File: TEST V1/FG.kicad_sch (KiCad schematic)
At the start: 34 parts, among them U10 MCP4725A2T-ECH, U2 AD9833, U3 LM318N, U4 LM318N, Y3 25 MHz

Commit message: Integrated FG, RPS, and PCB updates
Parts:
- C26: renamed from C12; footprint (none) -> Capacitor_SMD:C_0603_1608Metric_Pad1.08x0.95mm_HandSolder
- C27: renamed from C11; footprint (none) -> Capacitor_SMD:C_0603_1608Metric_Pad1.08x0.95mm_HandSolder
- C28: renamed from C6; footprint (none) -> Capacitor_SMD:C_0603_1608Metric_Pad1.08x0.95mm_HandSolder
- C29: renamed from C40; footprint (none) -> Capacitor_SMD:C_0603_1608Metric_Pad1.08x0.95mm_HandSolder
- C30: renamed from C9; footprint (none) -> Capacitor_SMD:C_0603_1608Metric_Pad1.08x0.95mm_HandSolder
- C31: renamed from C5; footprint (none) -> Capacitor_SMD:C_0603_1608Metric_Pad1.08x0.95mm_HandSolder
- C32: renamed from C10; footprint (none) -> Capacitor_SMD:C_0603_1608Metric_Pad1.08x0.95mm_HandSolder
- C33: renamed from C41; footprint (none) -> Capacitor_SMD:C_0603_1608Metric_Pad1.08x0.95mm_HandSolder
- C34: renamed from C8; footprint (none) -> Capacitor_SMD:C_0603_1608Metric_Pad1.08x0.95mm_HandSolder
- C35: renamed from C7; footprint (none) -> Capacitor_SMD:C_0603_1608Metric_Pad1.08x0.95mm_HandSolder
- C36: renamed from C20; footprint (none) -> Capacitor_SMD:C_0603_1608Metric_Pad1.08x0.95mm_HandSolder
- C37: renamed from C21; footprint (none) -> Capacitor_SMD:C_0603_1608Metric_Pad1.08x0.95mm_HandSolder
- R41: renamed from R10; footprint (none) -> Resistor_SMD:R_0603_1608Metric_Pad0.98x0.95mm_HandSolder
- R42: renamed from R2; footprint (none) -> Resistor_SMD:R_0603_1608Metric_Pad0.98x0.95mm_HandSolder
- R43: renamed from R1; footprint (none) -> Resistor_SMD:R_0603_1608Metric_Pad0.98x0.95mm_HandSolder
- R44: renamed from R9; footprint (none) -> Resistor_SMD:R_0603_1608Metric_Pad0.98x0.95mm_HandSolder
- R45: renamed from R57; footprint (none) -> Resistor_SMD:R_0603_1608Metric_Pad0.98x0.95mm_HandSolder
- R46: renamed from R14; footprint (none) -> Resistor_SMD:R_0603_1608Metric_Pad0.98x0.95mm_HandSolder
- R47: renamed from R12; footprint (none) -> Resistor_SMD:R_0603_1608Metric_Pad0.98x0.95mm_HandSolder
- R48: renamed from R7; footprint (none) -> Resistor_SMD:R_0603_1608Metric_Pad0.98x0.95mm_HandSolder
- R49: renamed from R8; footprint (none) -> Resistor_SMD:R_0603_1608Metric_Pad0.98x0.95mm_HandSolder
- R50: renamed from R4; footprint (none) -> Resistor_SMD:R_0603_1608Metric_Pad0.98x0.95mm_HandSolder
- R51: renamed from R3; footprint (none) -> Resistor_SMD:R_0603_1608Metric_Pad0.98x0.95mm_HandSolder
- R52: renamed from R13; footprint (none) -> Resistor_SMD:R_0603_1608Metric_Pad0.98x0.95mm_HandSolder
- R53: renamed from R6; footprint (none) -> Resistor_SMD:R_0603_1608Metric_Pad0.98x0.95mm_HandSolder
- R54: renamed from R11; footprint (none) -> Resistor_SMD:R_0603_1608Metric_Pad0.98x0.95mm_HandSolder
- R55: renamed from R5; footprint (none) -> Resistor_SMD:R_0603_1608Metric_Pad0.98x0.95mm_HandSolder
- R56: renamed from R26; footprint (none) -> Resistor_SMD:R_0603_1608Metric_Pad0.98x0.95mm_HandSolder
- renumbered U3 to U7, U2 to U8, U4 to U9, Y3 to Y2

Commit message: updated RPS schematic
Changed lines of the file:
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@@
 		)
 	)
+	(global_label "-12V"
+		(shape input)
+		(at 35.56 147.32 270)
+		(fields_autoplaced yes)
+		(effects
+			(font
+				(size 1.27 1.27)
+			)
+			(justify right)
+		)
+		(property "Intersheetrefs" "${INTERSHEET_REFS}"
+			(at 35.56 155.3852 90)
+			(effects
+				(font
+					(size 1.27 1.27)
+				)
+				(justify right)
+				(hide yes)
+			)
+		)
+	)
 	(global_label "5V"
 		(shape input)
@@
 		)
 	)
+	(global_label "3v3"
+		(shape input)
+		(at 107.95 25.4 0)
+		(fields_autoplaced yes)
+		(effects
+			(font
+				(size 1.27 1.27)
+			)
+			(justify left)
+		)
+		(property "Intersheetrefs" "${INTERSHEET_REFS}"
+			(at 114.3218 25.4 0)
+			(effects
+				(font
+					(size 1.27 1.27)
+				)
+				(justify left)
+				(hide yes)
+			)
+		)
+	)
 	(global_label "SPI_EN"
 		(shape output)
@@
 		(dnp no)
 		(property "Reference" "R41"
-			(at 37.084 149.352 90)
+			(at 42.164 145.034 90)
 			(effects
 				(font

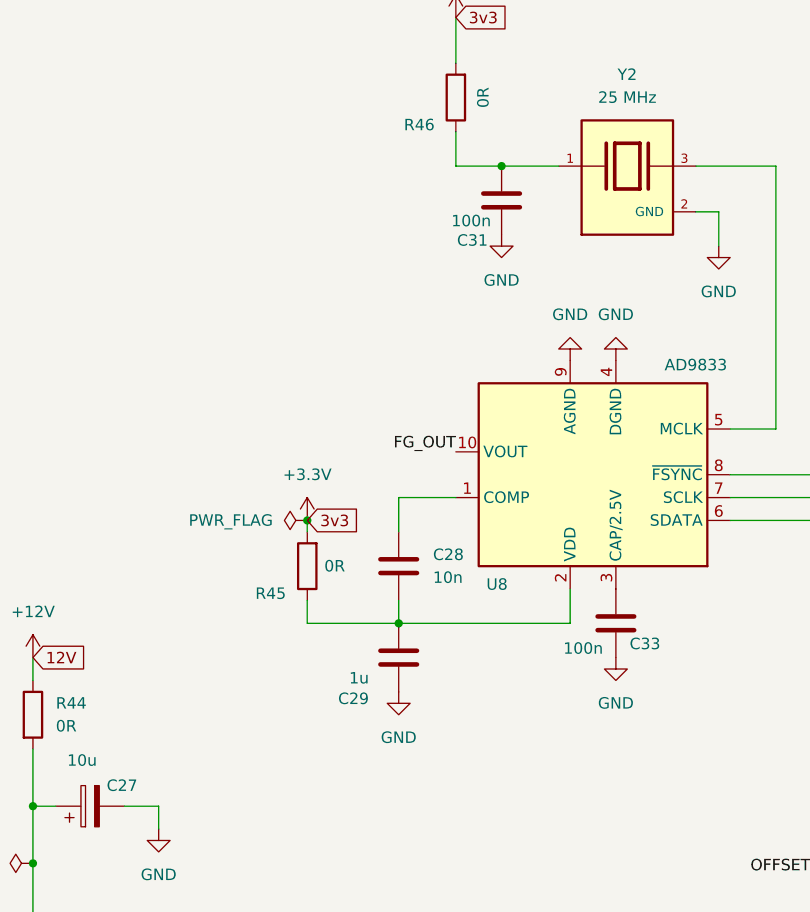
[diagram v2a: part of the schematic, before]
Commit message: updated schematic of FG
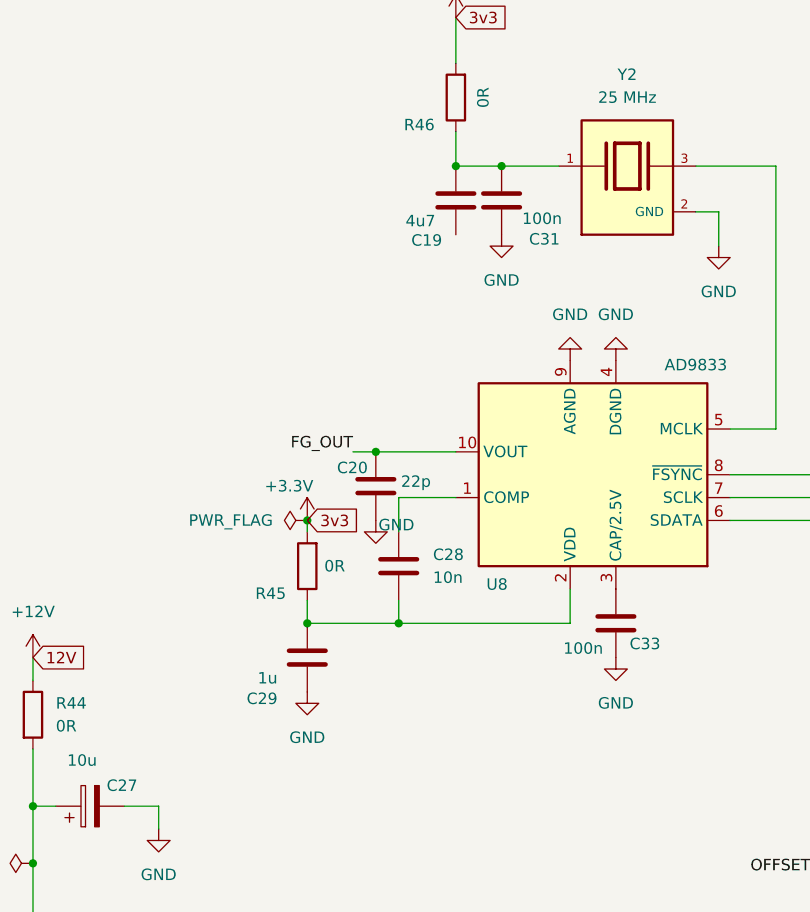
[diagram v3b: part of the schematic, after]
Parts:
- added C19: 4u7, Capacitor_SMD:C_0603_1608Metric_Pad1.08x0.95mm_HandSolder, symbol Device:C
- added C20: 22p, Capacitor_SMD:C_0603_1608Metric_Pad1.08x0.95mm_HandSolder, symbol Device:C
- RV1: footprint (none) -> Potentiometer_THT:Potentiometer_Bourns_3386X_Horizontal
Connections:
- net FG_OUT: now also C20.2
- net GND: now also C20.1
- net at C31.2, R46.1, Y2.1: now also C19.2
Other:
- moved on the sheet: C29

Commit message: updated RPS sch
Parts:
- added J16: Conn_Coaxial, symbol Connector:Conn_Coaxial
- renumbered C26 to C21, C27 to C22, C29 to C23, C20 to C24, C28 to C25, C19 to C26, C30 to C27, C31 to C28, C32 to C29, C33 to C30, C34 to C31, C35 to C32, C36 to C33, C37 to C34, R41 to R31, R42 to R32, R43 to R33, R44 to R34, R45 to R35, R46 to R36, R47 to R37, R48 to R38, R49 to R39, R50 to R40, R51 to R41, R52 to R42, R53 to R43, R54 to R44, R55 to R45, R56 to R46, U7 to U5, U8 to U6, U9 to U7, U10 to U8
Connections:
- net GND: now also C26.1, J16.2 (Ext)
- net U4_VOUT: now also J16.1 (In)

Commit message: minor changes
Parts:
- removed J16: Conn_Coaxial, symbol Connector:Conn_Coaxial
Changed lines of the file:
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@@
 	)
 	(label "U4_VOUT"
-		(at 200.66 135.89 90)
+		(at 200.66 135.89 0)
 		(effects
 			(font
@@
 	)
 	(symbol
-		(lib_id "power:GND")
-		(at 205.74 140.97 0)
-		(unit 1)
-		(exclude_from_sim no)
-		(in_bom yes)
-		(on_board yes)
-		(dnp no)
-		(property "Reference" "#PWR088"
-			(at 205.74 147.32 0)
-			(effects
-				(font
-					(size 1.27 1.27)
-				)
-				(hide yes)
-			)
-		)
-		(property "Value" "GND"
-			(at 201.93 142.748 0)
-			(effects
-				(font
-					(size 1.27 1.27)
-				)
-			)
-		)
-		(property "Footprint" ""
-			(at 205.74 140.97 0)
-			(effects
-				(font
-					(size 1.27 1.27)
-				)
-				(hide yes)
-			)
-		)
-		(property "Datasheet" ""
-			(at 205.74 140.97 0)
-			(effects
-				(font
-					(size 1.27 1.27)
-				)
-				(hide yes)
-			)
-		)
-		(property "Description" "Power symbol creates a global label with name \"GND\" , ground"
-			(at 205.74 140.97 0)
-			(effects
-				(font
-					(size 1.27 1.27)
-				)
-				(hide yes)
-			)
-		)
-		(pin "1"
-		)
-		(instances
-			(project "TEST V1"
-				(path "/e198004f-db65-4a52-ae89-6b1c9a9775ee/67a157b6-1f41-4621-8fe4-10cef685d6f6"
-					(reference "#PWR088")
-					(unit 1)
-				)
-			)
-		)
-	)
-	(symbol
 		(lib_id "Device:R")
 		(at 91.44 86.36 180)
@@
 					(unit 1)
 				)
-			)
-		)
-	)
-	(symbol
-		(lib_id "Connector:Conn_Coaxial")
-		(at 205.74 135.89 0)
-		(unit 1)
-		(exclude_from_sim no)
-		(in_bom yes)
-		(on_board yes)
-		(dnp no)
-		(fields_autoplaced yes)
-		(property "Reference" "J16"
-			(at 209.55 134.9131 0)
-			(effects
-				(font
-					(size 1.27 1.27)
-				)
-				(justify left)
-			)
-		)
-		(property "Value" "Conn_Coaxial"
-			(at 209.55 137.4531 0)
-			(effects
-				(font
-					(size 1.27 1.27)
-				)
-				(justify left)
-			)
-		)
-		(property "Footprint" ""
-			(at 205.74 135.89 0)
-			(effects
-				(font
-					(size 1.27 1.27)
-				)
-				(hide yes)
-			)
-		)
-		(property "Datasheet" "~"
-			(at 205.74 135.89 0)
-			(effects
-				(font
-					(size 1.27 1.27)
-				)
-				(hide yes)
-			)
-		)
-		(property "Description" "coaxial connector (BNC, SMA, SMB, SMC, Cinch/RCA, LEMO, ...)"
-			(at 205.74 135.89 0)
-			(effects
-				(font
-					(size 1.27 1.27)
-				)
-				(hide yes)
-			)
-		)
-		(pin "2"
-		)
-		(pin "1"
-		)
-		(instances
-			(project ""
-				(path "/e198004f-db65-4a52-ae89-6b1c9a9775ee/67a157b6-1f41-4621-8fe4-10cef685d6f6"
-					(reference "J16")
-					(unit 1)
-				)
